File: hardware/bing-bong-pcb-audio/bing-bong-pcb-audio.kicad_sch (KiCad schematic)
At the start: 55 parts, among them J1 Eurorack Power, J2 Conn_01x08_Pin, J3 Conn_01x08_Pin, Q1 2N3904, U1 SeeeduinoXIAO RA4M1, U2 L7805, U3 TL071, U4 TL074, U5 MCP6004

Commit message: changed cv resistor values
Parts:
- R11, R13, R19, R25: value 100k -> 300k
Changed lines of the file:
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@@
 			)
 		)
-		(property "Value" "100k"
+		(property "Value" "300k"
 			(at 84.074 123.952 90)
 			(effects
@@
 			)
 		)
-		(property "Value" "100k"
+		(property "Value" "300k"
 			(at 84.074 89.662 90)
 			(effects
@@
 			)
 		)
-		(property "Value" "100k"
+		(property "Value" "300k"
 			(at 84.074 55.372 90)
 			(effects
@@
 			)
 		)
-		(property "Value" "100k"
+		(property "Value" "300k"
 			(at 84.074 21.082 90)
 			(effects

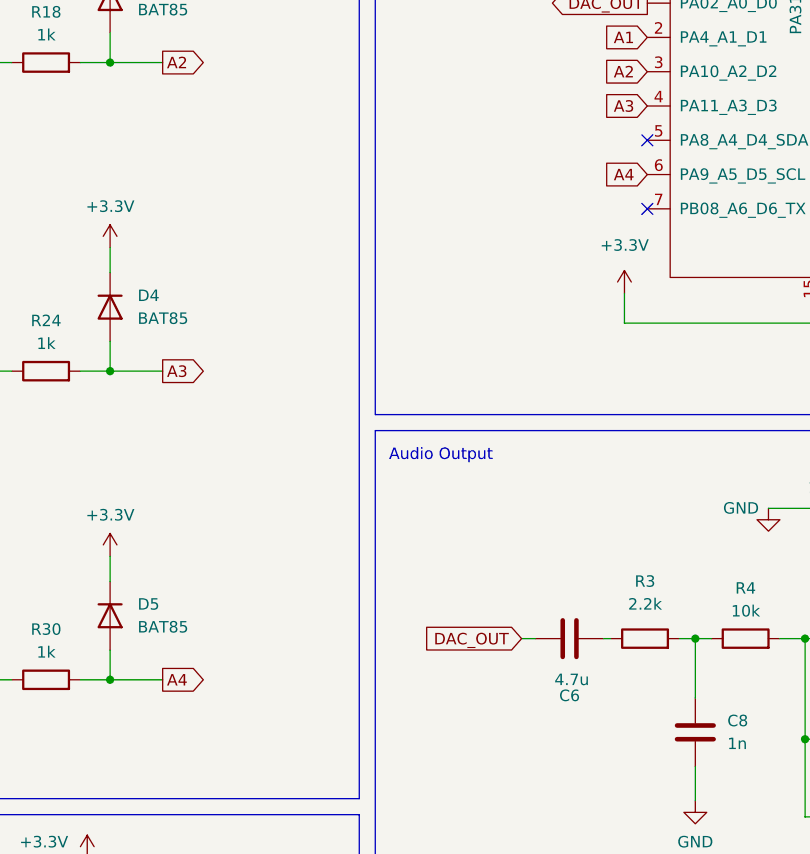
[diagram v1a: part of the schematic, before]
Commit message: corrected pin names
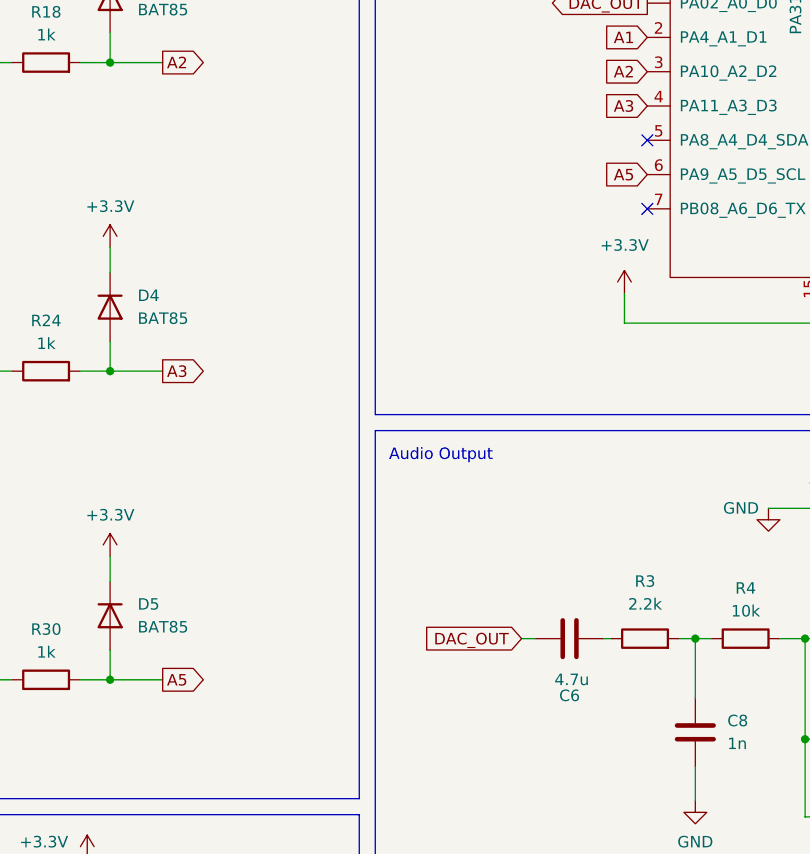
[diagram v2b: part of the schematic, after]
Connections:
- net A4 renamed A5
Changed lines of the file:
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@@
 		)
 	)
-	(global_label "A4"
+	(global_label "A5"
 		(shape output)
 		(at 153.67 142.24 0)
@@
 		)
 		(property "Intersheetrefs" "${INTERSHEET_REFS}"
-			(at 170.2624 142.24 0)
+			(at 158.9533 142.24 0)
 			(effects
 				(font
@@
 		)
 	)
-	(global_label "A4"
+	(global_label "A5"
 		(shape input)
 		(at 207.518 86.106 180)
@@
 		)
 		(property "Intersheetrefs" "${INTERSHEET_REFS}"
-			(at 190.9256 86.106 0)
-			(effects
-				(font
+			(at 202.2347 86.106 0)
+			(effects
+				(font
